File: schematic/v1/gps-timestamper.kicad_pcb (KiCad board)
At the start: 2 copper layers, 80 x 40 mm, 66 parts, among them J1 GPS, J2 Channel_0, J3 Channel_1, J4 USB_B, J5 SWD, U1 MCP603, U2 MCP603, U3 APU1206K-33, U4 MCP603, U5 MCP603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

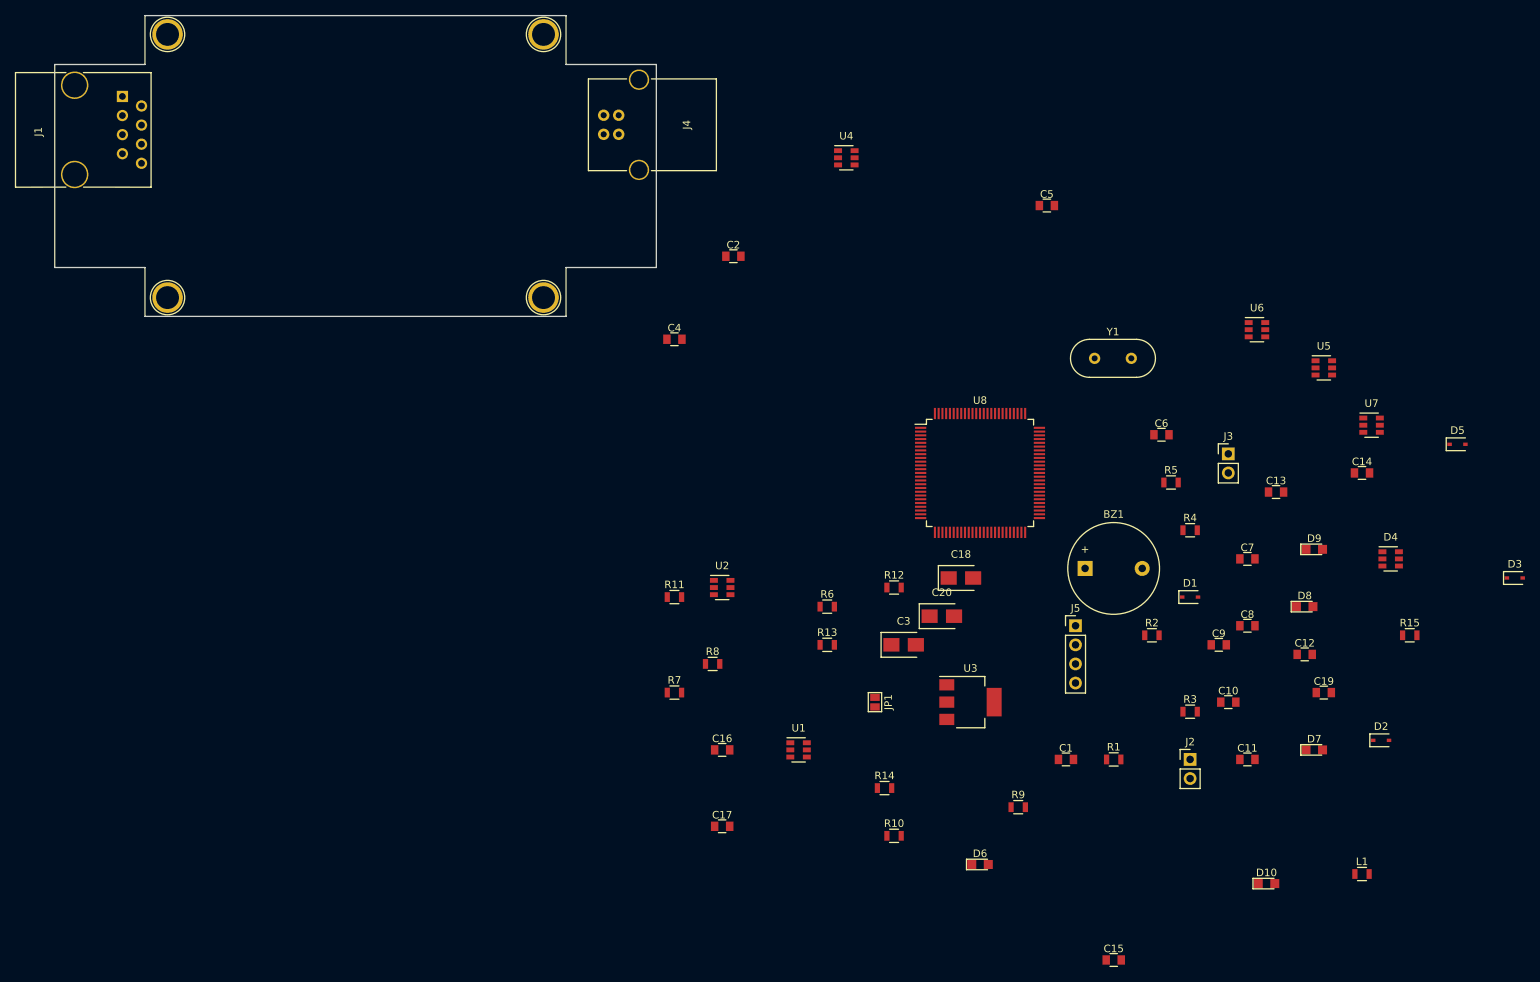
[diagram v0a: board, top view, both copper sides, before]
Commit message: [PCB] pcb seems done, silkscreen sims accurate
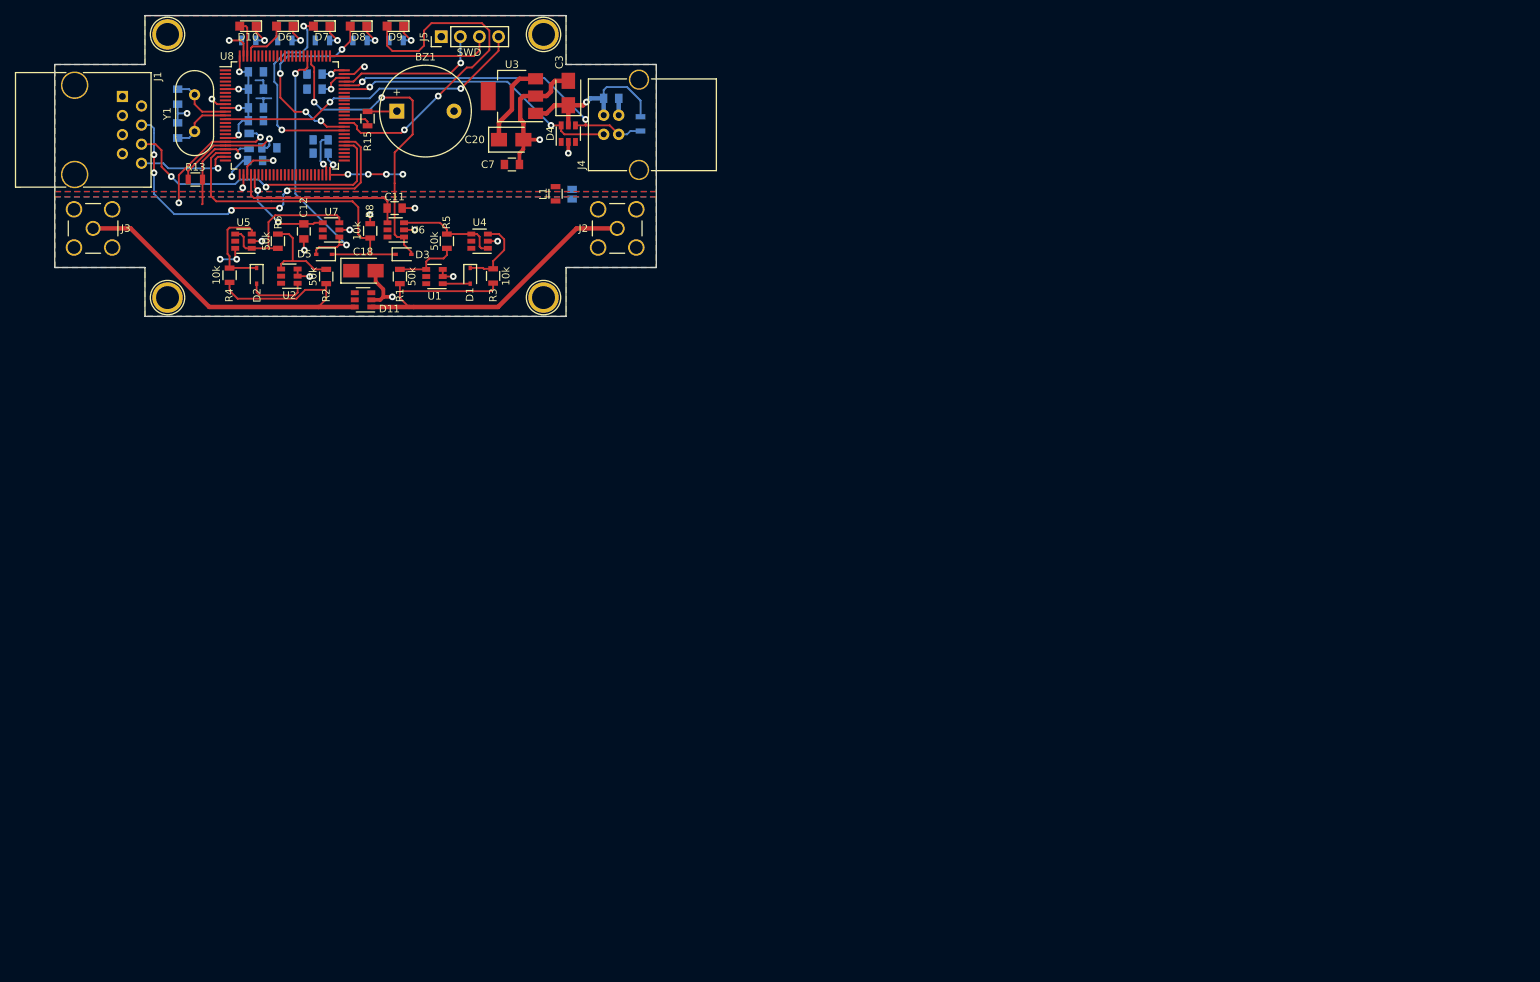
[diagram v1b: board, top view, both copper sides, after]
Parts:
- added D11: USBLC6-4SC6, TO_SOT_Packages_SMD:SOT-23-6, F.Cu at (64.0, 60.8)
- C1, C10, C13, C14, C15, C16, C17, C19, C2, C4, C5, C6, C8, C9, JP1, R10, R11, R12, R14, R7, R9: moved to B.Cu
- J2: value Channel_0 -> Channel0; footprint Pin_Headers:Pin_Header_Straight_1x02_Pitch2.54mm -> Connect:SMA_THT_Jack_Straight
- J3: value Channel_1 -> Channel1; footprint Pin_Headers:Pin_Header_Straight_1x02_Pitch2.54mm -> Connect:SMA_THT_Jack_Straight
- R8: value 5k -> 10k
- moved D10 177.1 mm to (48.7, 24.4), turned to 180 degrees
- moved D7 163.4 mm to (58.5, 24.4), turned to 180 degrees
- moved D2 161.8 mm to (49.9, 57.6), turned to 270 degrees
- moved C19 160.6 mm to (48.9, 39.7), turned to 90 degrees
- moved C15 157.2 mm to (57.5, 32.8), turned to 180 degrees
- moved R15 154.7 mm to (64.6, 36.7), turned to 90 degrees
- moved D3 153.9 mm to (69.4, 54.8)
- moved J3 153.9 mm to (28.1, 51.3)
- moved D5 152.8 mm to (58.8, 54.8), turned to 180 degrees
- moved C8 148.8 mm to (49.8, 35.3)
- moved D8 147.6 mm to (63.4, 24.4), turned to 180 degrees
- moved C14 145.4 mm to (58.4, 39.5), turned to 180 degrees
- moved D6 144.8 mm to (53.6, 24.4), turned to 180 degrees
- moved U5 144.7 mm to (48.1, 53.0), turned to 180 degrees
- moved C12 144.5 mm to (56.1, 51.7), turned to 270 degrees
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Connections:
- J2 pad 1: GND -> Net-(D11-Pad1)
- J2 pad 2: Net-(J2-Pad2) -> GNDA
- J3 pad 1: GND -> Net-(D11-Pad6)
- J3 pad 2: Net-(J3-Pad2) -> GNDA
- R1 pad 2: Net-(J2-Pad2) -> Net-(D11-Pad1)
- R2 pad 2: Net-(J3-Pad2) -> Net-(D11-Pad6)
- R3 pad 2: Net-(J2-Pad2) -> Net-(D11-Pad1)
- R4 pad 2: Net-(J3-Pad2) -> Net-(D11-Pad6)
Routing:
- net Net-(D11-Pad6): track 0.00 -> 57.5 mm
- net +3V3: track 0.00 -> 54.6 mm, vias 0 -> 11
- net Net-(D11-Pad1): track 0.00 -> 53.9 mm
- net GPS_MCU_RX: track 0.00 -> 48.9 mm, vias 0 -> 5
- net Net-(D9-Pad2): track 0.00 -> 46.8 mm, vias 0 -> 2
- net GND: track 0.00 -> 46.2 mm, vias 0 -> 8
- net USB_D+: track 0.00 -> 45.1 mm, vias 0 -> 2
- net Net-(D3-Pad2): track 0.00 -> 43.6 mm, vias 0 -> 2
- net TTL_IN: track 0.00 -> 43.6 mm
- net NRST: track 0.00 -> 42.0 mm, vias 0 -> 2
- net GNDA: track 0.00 -> 40.1 mm, vias 0 -> 12
- net GPS_MCU_TX: track 0.00 -> 39.3 mm, vias 0 -> 2
- net USB_D-: track 0.00 -> 38.2 mm, vias 0 -> 2
- net Net-(D5-Pad2): track 0.00 -> 35.0 mm, vias 0 -> 2
- net Net-(D7-Pad2): track 0.00 -> 27.2 mm, vias 0 -> 2
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- added copper zone on F.Cu, net +3.3VA
- added copper zone on F.Cu, net +3V3
- added copper zone on B.Cu, net GND
- added copper zone on B.Cu, net GNDA
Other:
- net class Default: via_dia 0.6 -> 0.9

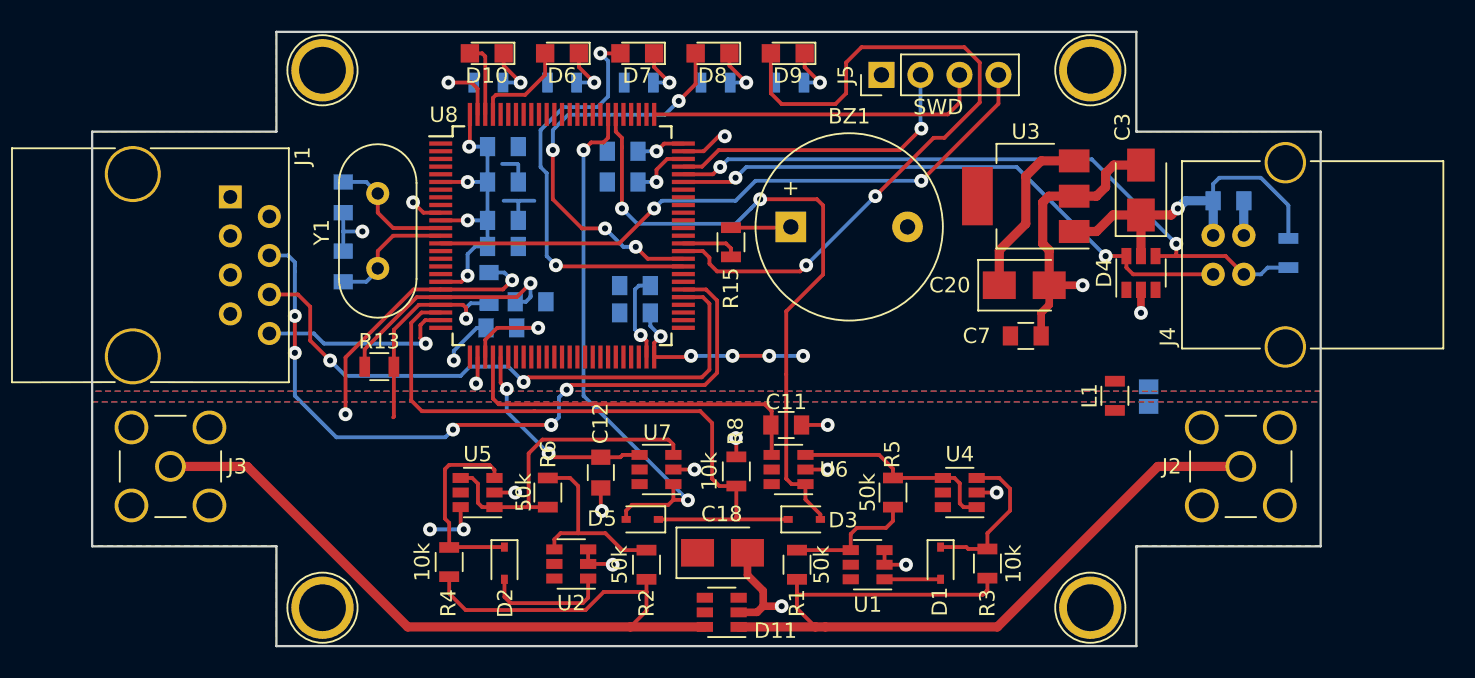
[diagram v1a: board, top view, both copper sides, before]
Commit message: [PCB] Design improved. RJ-45 input, buffered PPS output
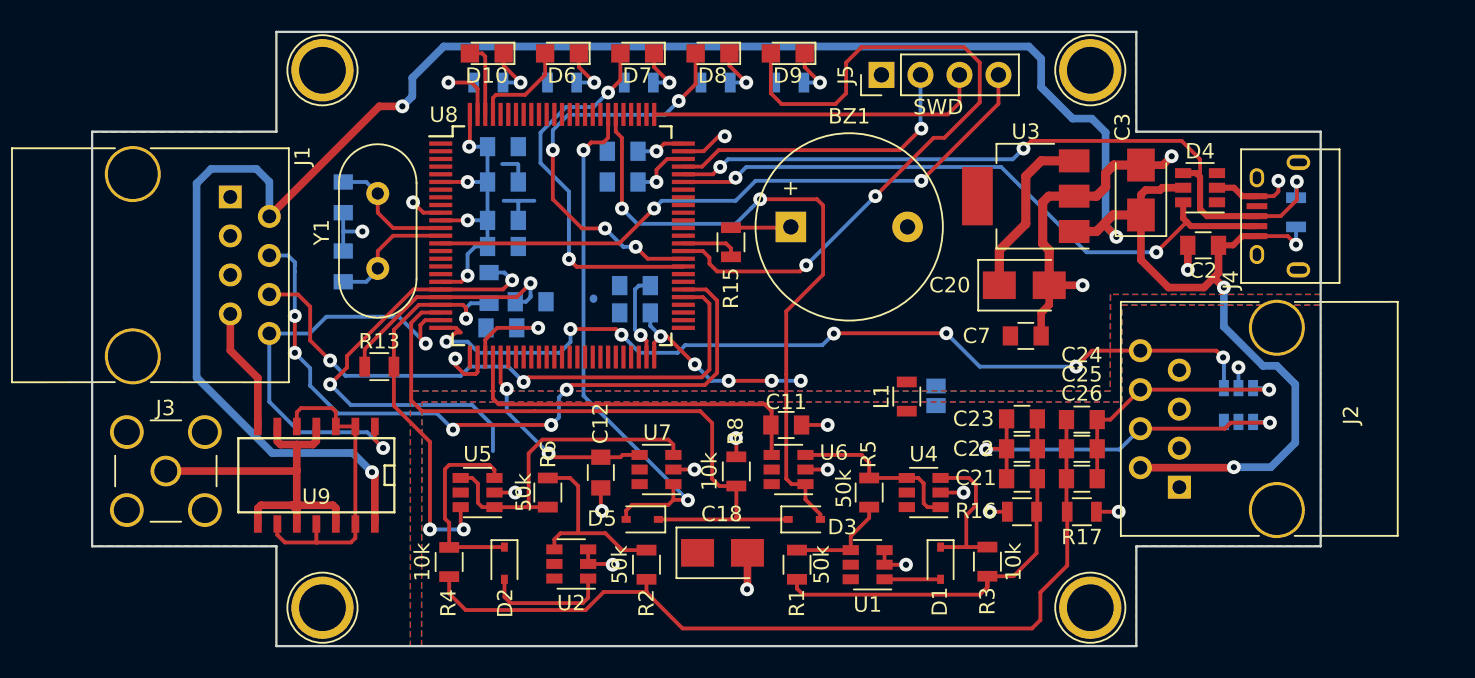
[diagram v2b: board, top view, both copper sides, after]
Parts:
- added C21: 10uF, Capacitors_SMD:C_0805, F.Cu at (83.5, 52.1)
- added C22: 10uF, Capacitors_SMD:C_0805, F.Cu at (83.5, 50.1)
- added C23: 10uF, Capacitors_SMD:C_0805, F.Cu at (83.5, 48.2)
- added C24: 10uF, Capacitors_SMD:C_0805, F.Cu at (87.5, 48.2)
- added C25: 10uF, Capacitors_SMD:C_0805, F.Cu at (87.5, 50.1)
- added C26: 10uF, Capacitors_SMD:C_0805, F.Cu at (87.5, 52.1)
- added R16: 1k, Resistors_SMD:R_0805, F.Cu at (83.5, 54.2)
- added R17: 1k, Resistors_SMD:R_0805, F.Cu at (87.5, 54.2)
- added U9: 74HC04, SMD_Packages:SOIC-14_N, F.Cu at (37.6, 52.0)
- C2: moved to F.Cu
- D11: moved to B.Cu
- J2: value Channel0 -> Input; footprint Connect:SMA_THT_Jack_Straight -> Connect:RJ45_8
- J3: value Channel1 -> PPS_OUT
- J4: value USB_B -> USB_OTG; footprint Connect:USB_B -> Connect:USB_Micro-B
- moved D11 36.3 mm to (97.7, 47.3), turned to 90 degrees
- moved JP1 13.9 mm to (78.0, 46.7)
- moved L1 13.6 mm to (76.0, 46.8)
- moved D4 6.75 mm to (95.2, 33.1), turned to 180 degrees
- moved J4 4.38 mm to (100.2, 35.0), turned to 90 degrees
- moved J2 4.22 mm to (93.8, 52.6), turned to 90 degrees
- moved C2 3.34 mm to (95.3, 36.9), turned to 180 degrees
- moved R7 2.70 mm to (101.4, 34.8), turned to 270 degrees
- moved U4 2.35 mm to (77.2, 53.0)
- moved R5 1.55 mm to (73.6, 53.0)
- moved J3 0.42 mm to (27.8, 51.6)
- moved R3 0.12 mm to (81.3, 57.5)
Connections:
- D11 pad 1: Net-(D11-Pad1) -> Net-(C21-Pad2)
- D11 pad 4: Net-(D11-Pad4) -> UART_TAG_TX
- D11 pad 6: Net-(D11-Pad6) -> Net-(C24-Pad2)
- J1 pad 2: +3V3 -> +5V
- J2 pad 1: Net-(D11-Pad1) -> GNDA
- J2 pad 2: GNDA -> +5V
- J3 pad 1: Net-(D11-Pad6) -> Net-(J3-Pad1)
- J3 pad 2: GNDA -> GND
- J4 pad 4: GND -> Net-(J4-Pad4)
- J4 pad 5: Net-(J4-Pad5) -> GND
- R1 pad 2: Net-(D11-Pad1) -> Ch0_to_amp
- R2 pad 2: Net-(D11-Pad6) -> Ch1_to_amp
- R3 pad 2: Net-(D11-Pad1) -> Ch0_to_amp
- R4 pad 2: Net-(D11-Pad6) -> Ch1_to_amp
- U8 pad 25: Net-(U8-Pad25) -> UART_TAG_TX
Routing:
- net +5V: track 23.9 -> 160.5 mm, vias 1 -> 6
- net UART_TAG_TX: track 0.00 -> 59.3 mm, vias 0 -> 7
- net Net-(D11-Pad6): track 57.5 -> 0.00 mm
- net Ch1_to_amp: track 0.00 -> 56.4 mm
- net Net-(D11-Pad1): track 53.9 -> 0.00 mm
- net Ch0_to_amp: track 0.00 -> 27.2 mm
- net Net-(J3-Pad1): track 0.00 -> 26.7 mm
- net Net-(C21-Pad2): track 0.00 -> 25.6 mm, vias 0 -> 2
- net Net-(U9-Pad11): track 0.00 -> 20.5 mm
- net Net-(C24-Pad2): track 0.00 -> 17.0 mm, vias 0 -> 1
- net PPS_IN: track 13.3 -> 28.9 mm, vias 1 -> 2
- net GND: track 46.2 -> 57.4 mm, vias 8 -> 9
- net GNDA: track 40.1 -> 50.2 mm, vias 12 -> 14
- net +3.3VA: track 17.9 -> 27.5 mm, vias 3 -> 4
- net USB_D-: track 38.2 -> 42.4 mm
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
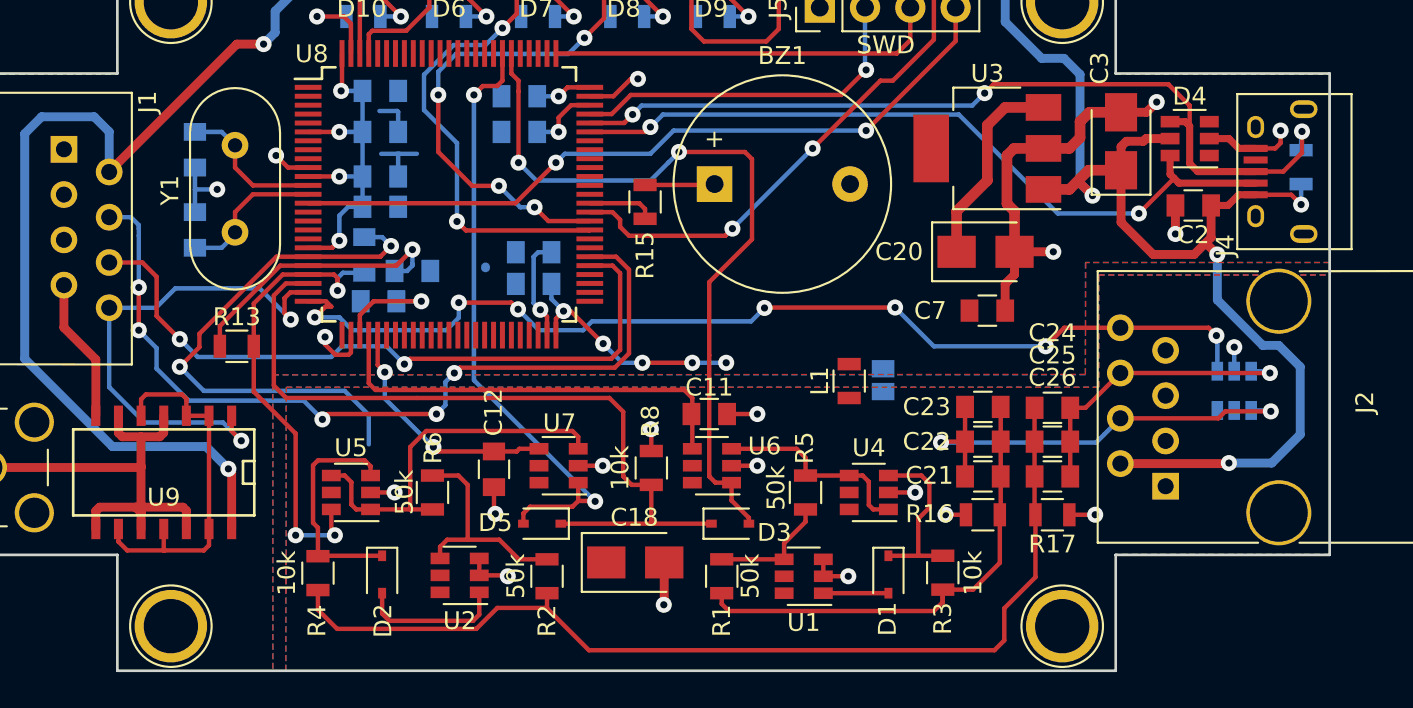
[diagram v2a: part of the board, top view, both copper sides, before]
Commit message: [PCB] Antenna done and input trigger output added for main device
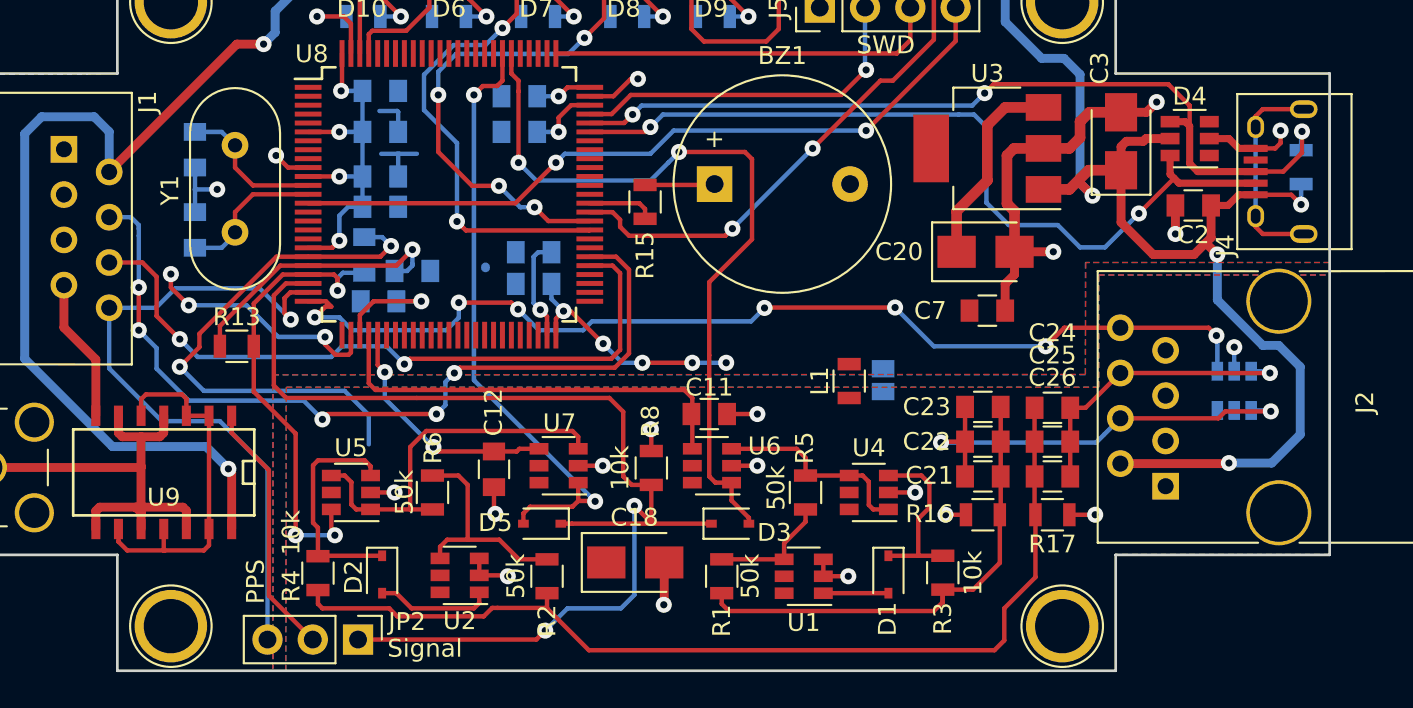
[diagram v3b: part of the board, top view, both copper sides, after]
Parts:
- added JP2: Out_select, Pin_Headers:Pin_Header_Straight_1x03_Pitch2.54mm, F.Cu at (48.5, 61.2)
- U1, U2, U4, U5, U6, U7: value MCP603 -> MCP633
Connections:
- U9 pad 1: PPS_IN -> Net-(JP2-Pad2)
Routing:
- net TTL_IN: track 43.6 -> 66.6 mm, vias 0 -> 2
- net Net-(JP2-Pad2): track 0.00 -> 14.4 mm
- net Net-(J4-Pad6): track 0.00 -> 11.9 mm
- net GND: track 57.4 -> 68.0 mm, vias 9 -> 11
- net PPS_IN: track 28.9 -> 38.4 mm, vias 2 -> 1
- net USB_D-: track 42.4 -> 46.4 mm
- net Net-(D2-Pad2): track 8.16 -> 6.53 mm
- net Ch1_to_amp: track 56.4 -> 55.6 mm
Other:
- board text added: "PPS"
- board text added: "Signal"
